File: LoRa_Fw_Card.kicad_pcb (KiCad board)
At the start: 2 copper layers, 26 x 30 mm, 15 parts, among them P1 USB_C_Plug_USB2.0, P2 60312202114513, P3 Conn_01x04_Male, U1 AP2112K-3.3, U2 RP2040TR7, U3 SX1276IMLTRT

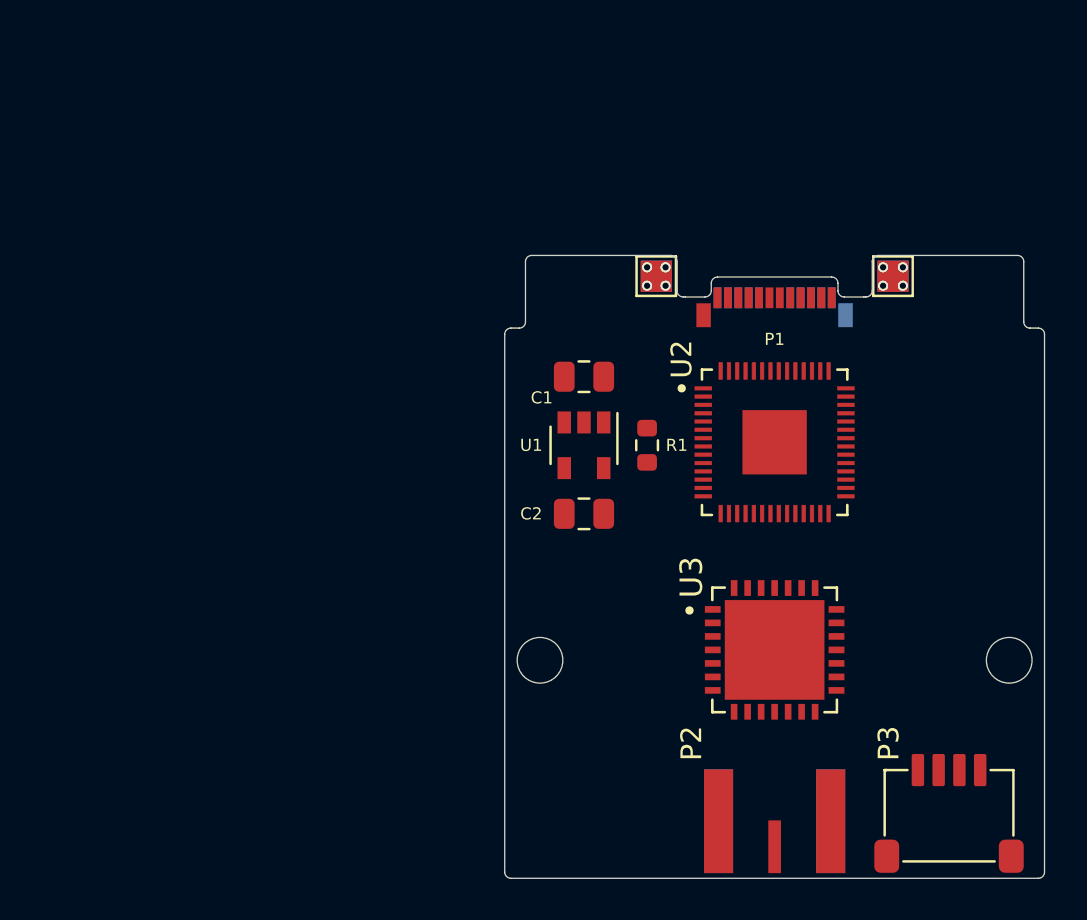
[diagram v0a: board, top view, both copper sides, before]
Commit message: Add partial RF and Memory wiring and placement
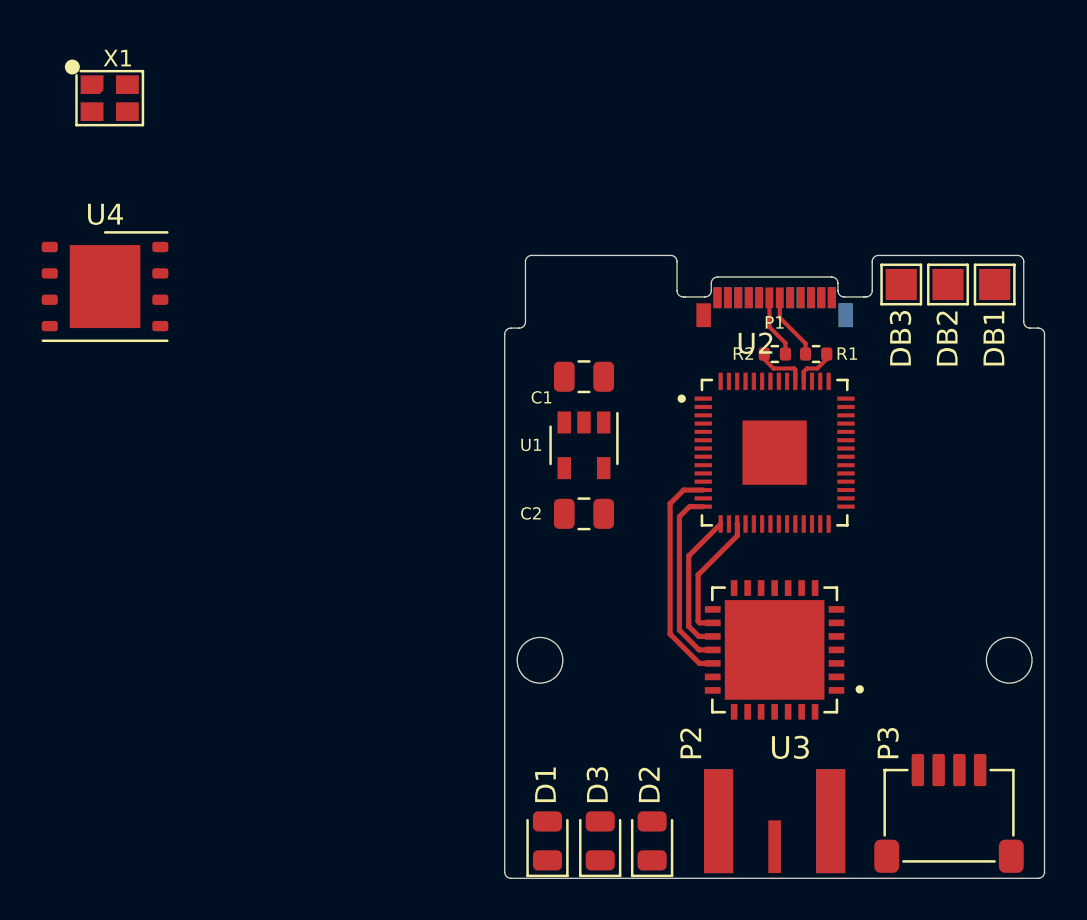
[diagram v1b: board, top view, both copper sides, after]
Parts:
- removed TP1, TP2, TP3, TP4: TestPoint, TestPoint:TestPoint_Pad_1.5x1.5mm
- added D1: LED, LED_SMD:LED_0805_2012Metric, F.Cu at (129.1, 155.2)
- added D2: LED, LED_SMD:LED_0805_2012Metric, F.Cu at (134.1, 155.2)
- added D3: LED, LED_SMD:LED_0805_2012Metric, F.Cu at (131.6, 155.2)
- added DB1: TestPoint, TestPoint:TestPoint_Pad_1.5x1.5mm, F.Cu at (150.6, 128.4)
- added DB2: TestPoint, TestPoint:TestPoint_Pad_1.5x1.5mm, F.Cu at (148.3, 128.4)
- added DB3: TestPoint, TestPoint:TestPoint_Pad_1.5x1.5mm, F.Cu at (146.1, 128.4)
- added R2: R_Small, Resistor_SMD:R_0402_1005Metric, F.Cu at (140.0, 131.8)
- added U4: W25Q128JVS, Package_SON:WSON-8-1EP_6x5mm_P1.27mm_EP3.4x4mm, F.Cu at (107.8, 128.5)
- added X1: WE-SPXO Crystal Osc 12.00MHz, KKicadLib:Oscillator_SMD_4pin_2.5x2.0mm, F.Cu at (108.0, 119.4)
- R1: value 5.1k -> R_Small; footprint Resistor_SMD:R_0603_1608Metric -> Resistor_SMD:R_0402_1005Metric
- moved R1 9.25 mm to (142.0, 131.8), turned to 0 degrees
- moved U2 0.50 mm to (140.0, 136.5)
- turned U3 to 180 degrees
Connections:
- P1 pad A6: /USB_DP -> /Power/D+
- P1 pad A7: /USB_DN -> /Power/D-
- R1 pad 1: Net-(P1-PadA5) -> /Power/D-
- R1 pad 2: GND -> /MCU Core/USB_DN
- U2 pad 1: Net-(U2-Pad1) -> +3V3
- U2 pad 10: Net-(U2-Pad1) -> +3V3
- U2 pad 12: unconnected-(U2-Pad12) -> /MCU Core/RF_CS_N
- U2 pad 14: unconnected-(U2-Pad14) -> /MCU Core/RF_MOSI
- U2 pad 15: unconnected-(U2-Pad15) -> /MCU Core/RF_MISO
- U2 pad 17: unconnected-(U2-Pad17) -> /MCU Core/RF_SCLK
- U2 pad 19: unconnected-(U2-Pad19) -> GND
- U2 pad 20: unconnected-(U2-Pad20) -> /MCU Core/XOSC
- U2 pad 22: Net-(U2-Pad1) -> +3V3
- U2 pad 23: Net-(U2-Pad23) -> +1V1
- U2 pad 24: unconnected-(U2-Pad24) -> Net-(TP3-Pad1)
- U2 pad 25: unconnected-(U2-Pad25) -> Net-(TP4-Pad1)
- U2 pad 28: unconnected-(U2-Pad28) -> /MCU Core/RF_DIO0
- U2 pad 29: unconnected-(U2-Pad29) -> /MCU Core/RF_DIO1
- U2 pad 30: unconnected-(U2-Pad30) -> /MCU Core/RF_DIO2
- U2 pad 31: unconnected-(U2-Pad31) -> /MCU Core/RF_DIO3
- U2 pad 32: unconnected-(U2-Pad32) -> /MCU Core/RF_DIO4
- U2 pad 33: Net-(U2-Pad1) -> +3V3
- U2 pad 34: unconnected-(U2-Pad34) -> /MCU Core/RF_DIO5
- U2 pad 35: unconnected-(U2-Pad35) -> /MCU Core/RF_RST_N
- U2 pad 42: Net-(U2-Pad1) -> +3V3
- U2 pad 43: unconnected-(U2-Pad43) -> +3V3
- U2 pad 44: unconnected-(U2-Pad44) -> +3V3
- U2 pad 45: unconnected-(U2-Pad45) -> +1V1
- U2 pad 46: unconnected-(U2-Pad46) -> /MCU Core/USB_DN
- U2 pad 47: unconnected-(U2-Pad47) -> /MCU Core/USB_DP
- U2 pad 48: unconnected-(U2-Pad48) -> +3V3
- U2 pad 49: Net-(U2-Pad1) -> +3V3
- U2 pad 50: Net-(U2-Pad23) -> +1V1
- U2 pad 51: unconnected-(U2-Pad51) -> /MCU Core/MEM_D3
- U2 pad 52: unconnected-(U2-Pad52) -> /MCU Core/MEM_CLK
- U2 pad 53: unconnected-(U2-Pad53) -> /MCU Core/MEM_D0
- U2 pad 54: unconnected-(U2-Pad54) -> /MCU Core/MEM_D2
- U2 pad 55: unconnected-(U2-Pad55) -> /MCU Core/MEM_D1
- U2 pad 56: unconnected-(U2-Pad56) -> /MCU Core/MEM_CS_N
- U3 pad 10: unconnected-(U3-Pad10) -> /MCU Core/RF_DIO2
- U3 pad 11: unconnected-(U3-Pad11) -> /MCU Core/RF_DIO3
- U3 pad 12: unconnected-(U3-Pad12) -> /MCU Core/RF_DIO4
- U3 pad 13: unconnected-(U3-Pad13) -> /MCU Core/RF_DIO5
- U3 pad 15: Net-(U3-Pad15) -> GND
- U3 pad 16: unconnected-(U3-Pad16) -> /MCU Core/RF_SCLK
- U3 pad 17: unconnected-(U3-Pad17) -> /MCU Core/RF_MISO
- U3 pad 18: unconnected-(U3-Pad18) -> /MCU Core/RF_MOSI
- U3 pad 19: unconnected-(U3-Pad19) -> /MCU Core/RF_CS_N
- U3 pad 23: Net-(U3-Pad15) -> GND
- U3 pad 26: Net-(U3-Pad15) -> GND
- U3 pad 29: Net-(U3-Pad15) -> GND
- U3 pad 7: unconnected-(U3-Pad7) -> /MCU Core/RF_RST_N
- U3 pad 8: unconnected-(U3-Pad8) -> /MCU Core/RF_DIO0
- U3 pad 9: unconnected-(U3-Pad9) -> /MCU Core/RF_DIO1
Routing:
- net /MCU Core/RF_CS_N: track 0.00 -> 10.8 mm
- net /MCU Core/RF_MOSI: track 0.00 -> 8.82 mm
- net /MCU Core/RF_MISO: track 0.00 -> 6.92 mm
- net /MCU Core/RF_SCLK: track 0.00 -> 6.23 mm
- net /Power/D-: track 0.00 -> 3.22 mm
- net /Power/D+: track 0.00 -> 3.03 mm
- net /MCU Core/USB_DP: track 0.00 -> 2.52 mm
- net /MCU Core/USB_DN: track 0.00 -> 2.07 mm
- net GND: vias 8 -> 0
